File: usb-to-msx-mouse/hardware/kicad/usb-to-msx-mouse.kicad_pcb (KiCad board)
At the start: 2 copper layers, 52 x 22 mm, 34 parts, among them J1 USB_A, J2 DB9_Male, SW1 BOOTSEL, U1 RP2040, U2 W25Q16, U3 74HCT245, U4 XC6206, Y1 12MHz

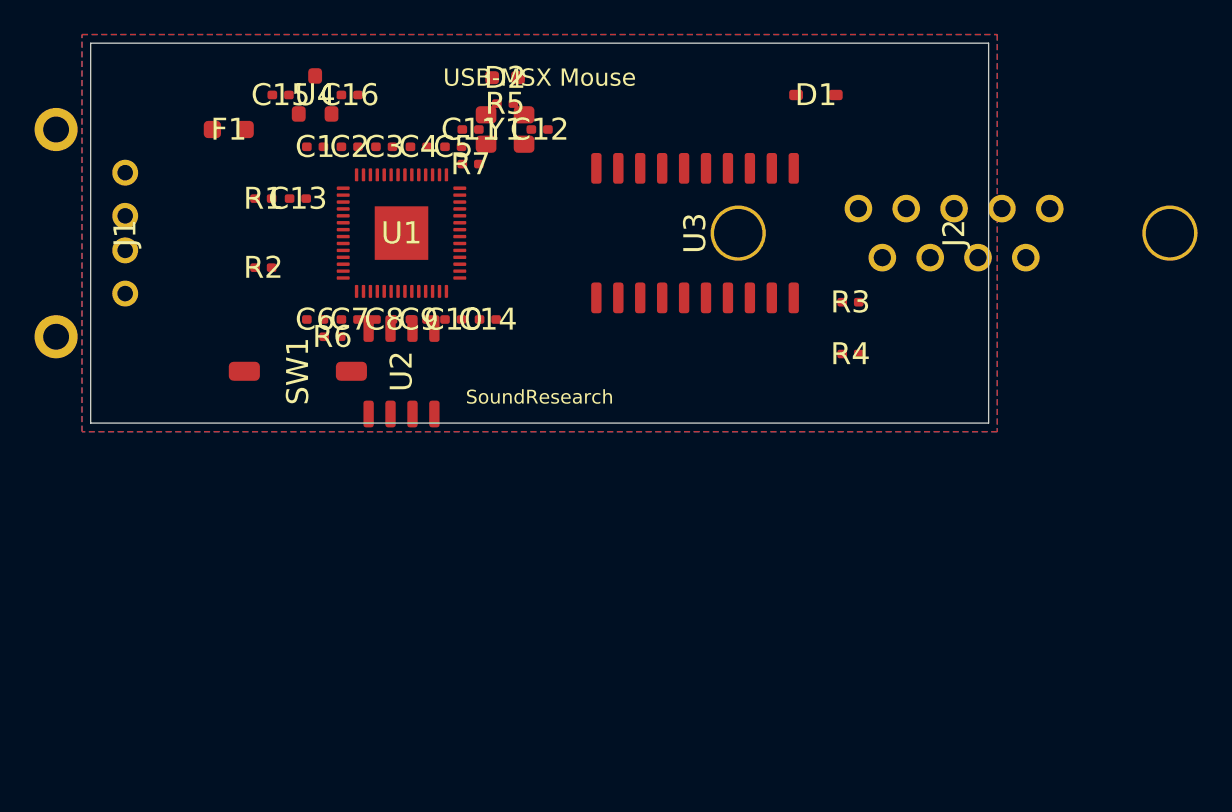
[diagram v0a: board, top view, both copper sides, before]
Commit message: Archive: first USB-to-MSX attempt (S-expression generator, KiCad 9 gotchas, Quilter outputs, kicad-cli validation). Superseded by Sound-Research/SR-usb-to-msx; kept for its learnings.
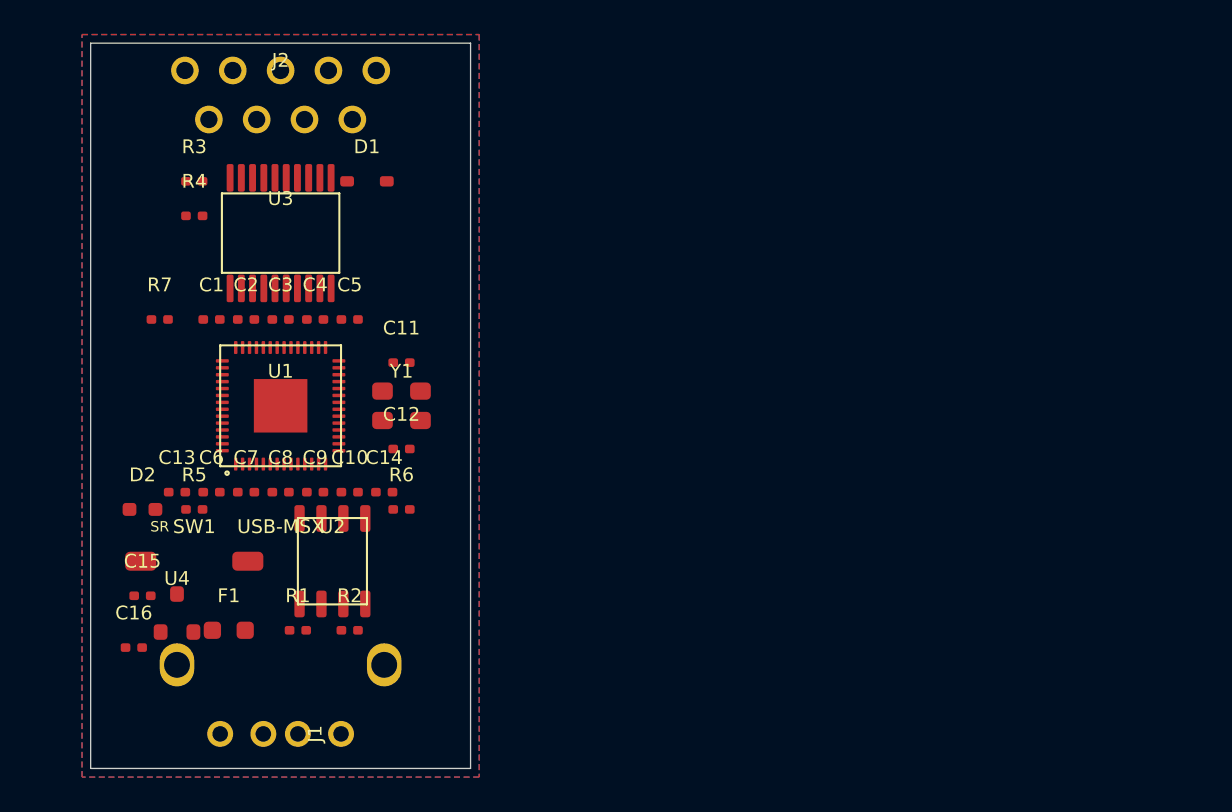
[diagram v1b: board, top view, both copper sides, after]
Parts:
- C1, C10, C11, C12, C13, C14, C15, C16, C2, C3, C4, C5, C6, C7, C8, C9, R1, R2, R3, R4, R5, R6, R7: footprint (none) -> Resistor_SMD:R_0402_1005Metric
- D1: footprint (none) -> Diode_SMD:D_SOD-323
- D2: footprint (none) -> LED_SMD:LED_0603_1608Metric
- F1: footprint (none) -> Fuse:Fuse_0805_2012Metric
- J1: footprint (none) -> Connector_USB:USB_A_Molex_67643_Horizontal
- J2: footprint (none) -> Connector_Dsub:DSUB-9_Male_Horizontal_P2.77x2.84mm_EdgePinOffset7.70mm
- SW1: footprint (none) -> Button_Switch_SMD:SW_SPST_TL3342
- U1: footprint (none) -> Package_DFN_QFN:QFN-56-1EP_7x7mm_P0.4mm
- U2: footprint (none) -> Package_SO:SOIC-8_3.9x4.9mm_P1.27mm
- U3: footprint (none) -> Package_SO:TSSOP-20_4.4x6.5mm_P0.65mm
- U4: footprint (none) -> Package_TO_SOT_SMD:SOT-23
- Y1: footprint (none) -> Crystal:Crystal_SMD_3225-4Pin_3.2x2.5mm
- moved J2 39.8 mm to (111.0, 103.0), turned to 0 degrees
- moved R4 38.8 mm to (106.0, 110.0)
- moved R3 38.6 mm to (106.0, 108.0)
- moved C16 34.4 mm to (102.5, 135.0)
- moved D2 32.6 mm to (103.0, 127.0)
- moved U4 31.0 mm to (105.0, 133.0)
- moved J1 30.4 mm to (111.0, 140.0), turned to 270 degrees
- moved C15 30.1 mm to (103.0, 132.0)
- moved R5 29.6 mm to (106.0, 127.0)
- moved F1 29.0 mm to (108.0, 134.0)
- moved D1 26.5 mm to (116.0, 108.0)
- moved R1 25.1 mm to (112.0, 134.0)
- moved U3 24.0 mm to (111.0, 111.0), turned to 0 degrees
- moved R2 21.6 mm to (115.0, 134.0)
- moved C12 20.2 mm to (118.0, 123.5)
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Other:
- board size 52 x 22 mm -> 22 x 42 mm
- board text added: "SR"
- board text added: "USB-MSX"
- board text removed: "SoundResearch"
- board text removed: "USB-MSX Mouse"
